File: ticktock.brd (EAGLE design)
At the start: 61 x 67.3 mm, 66 parts, among them IC1 ATMEGA644A, IC2 AD8611, IC3 REF200, IC4 OPA381, J1 ISP PGMR, Q1 MOSFET-NCHANNEL2N7002PW, Q2 MOSFET-NCHANNELBSS138, Q3 MOSFET-NCHANNELBSS138, U1 MAX232, U2 XTAL, U3 FT232, U4 BMP180, X2 DB9 Male

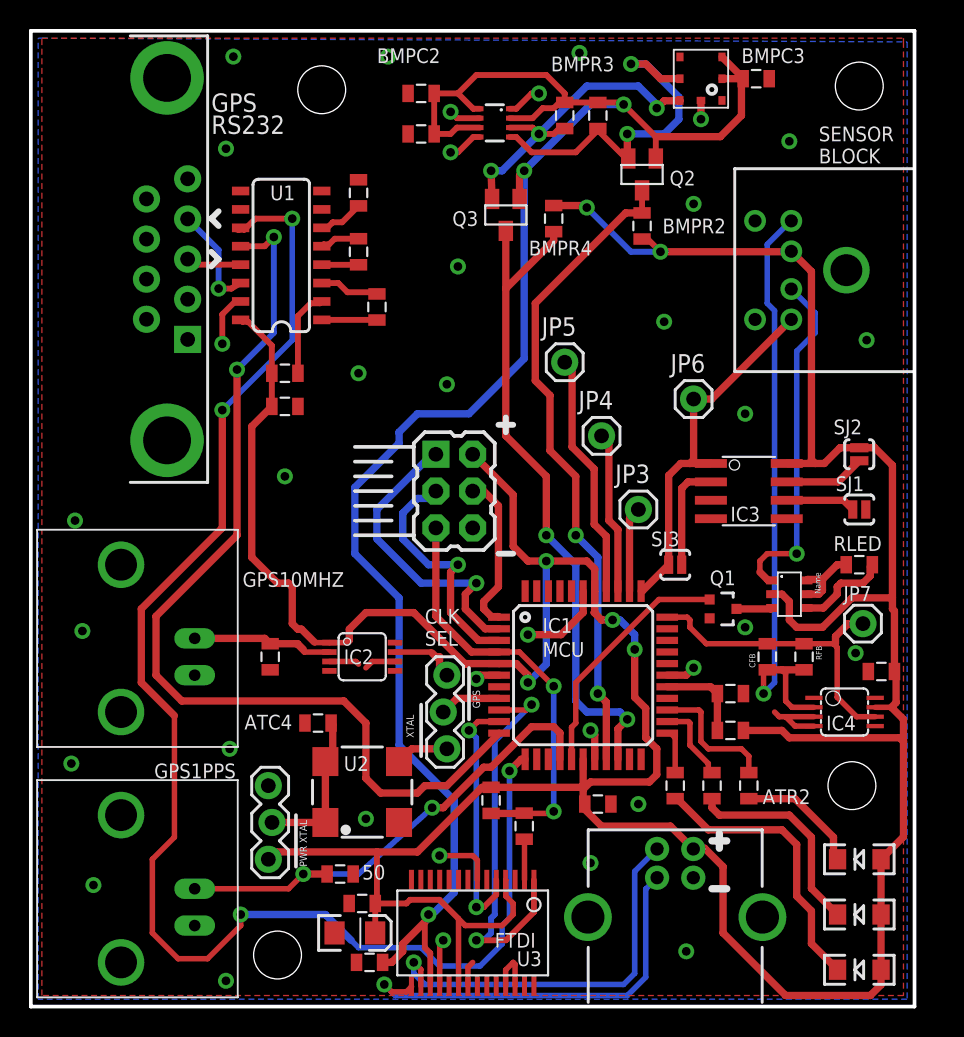
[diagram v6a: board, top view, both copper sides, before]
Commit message: Shuffle tight parts/silkscreens around
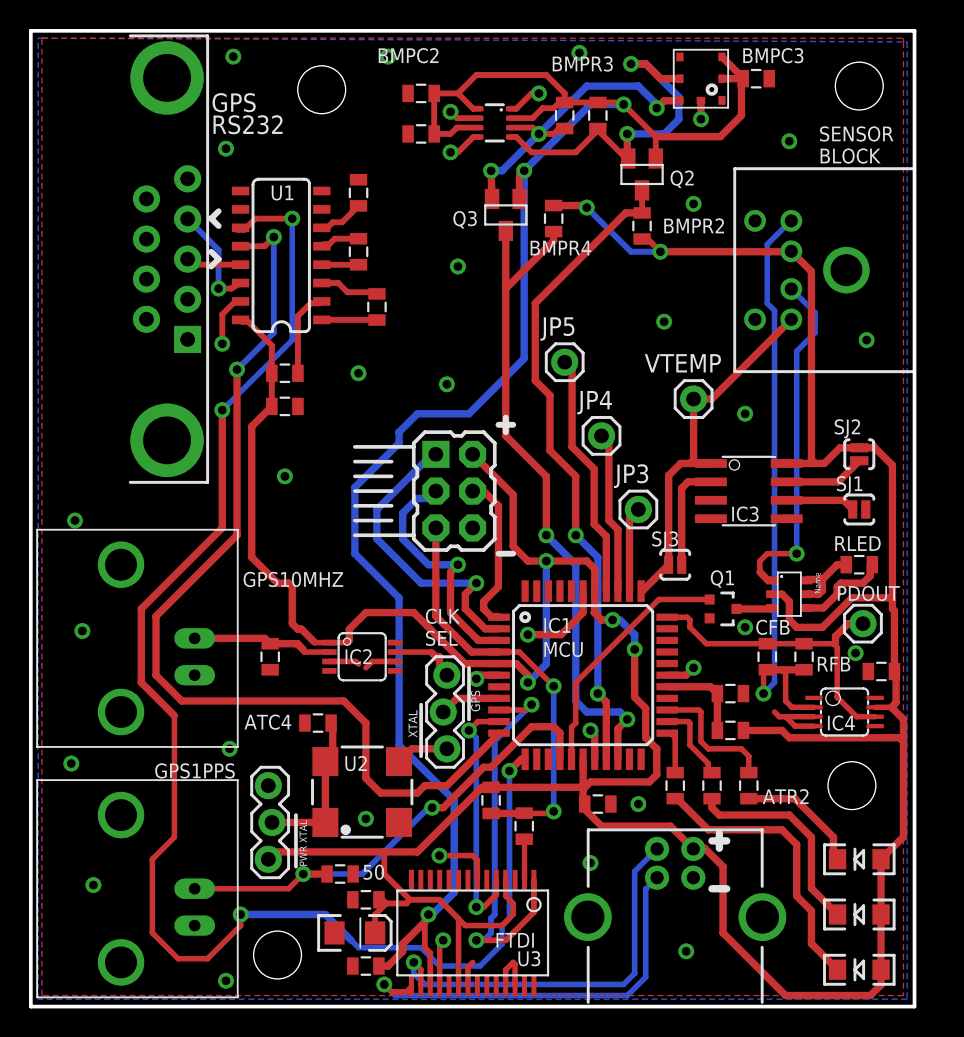
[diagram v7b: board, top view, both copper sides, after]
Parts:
- moved FTC1 0.36 mm to (23.1, 7.37)
- moved FTC3 0.36 mm to (23.1, 2.79)
- renumbered JP6 to VTEMP, JP7 to PDOUT
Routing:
- net 5V: track 272.9 -> 274.0 mm

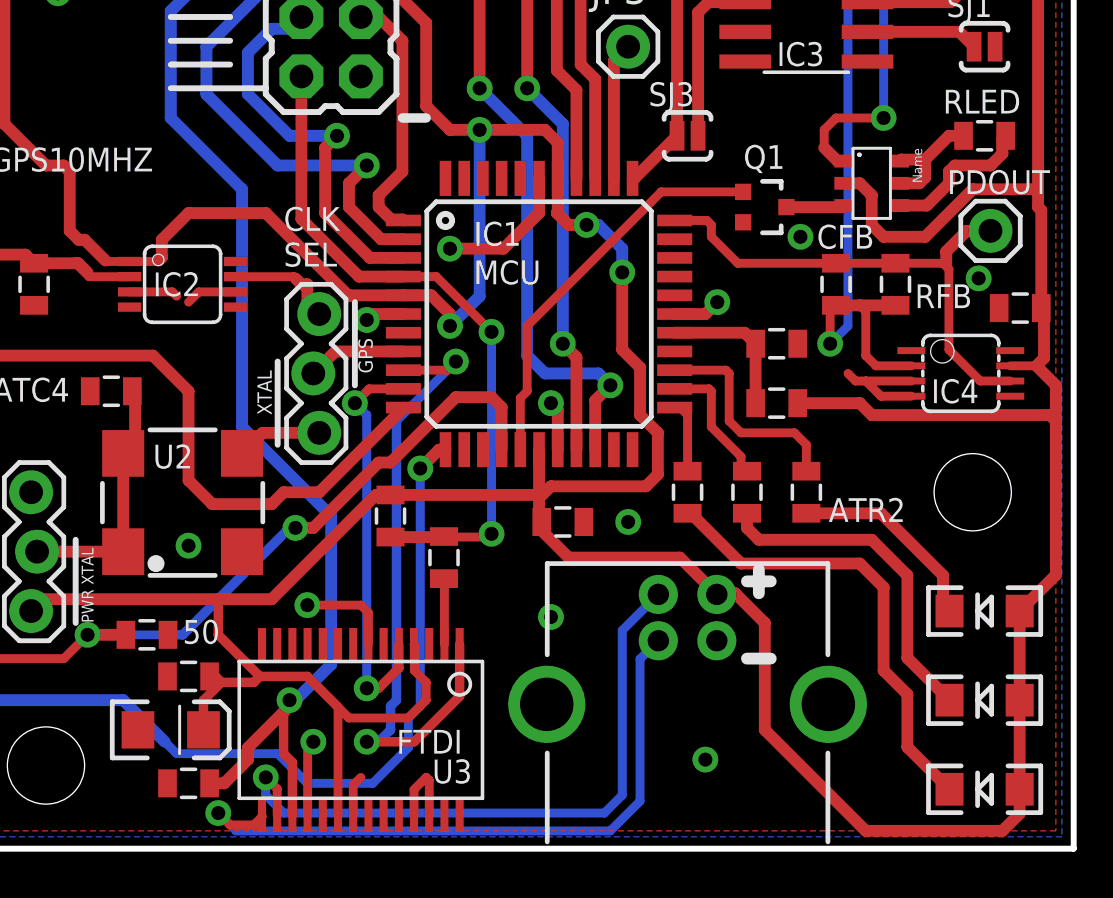
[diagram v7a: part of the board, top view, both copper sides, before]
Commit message: Modify Silkscreen for AL5802
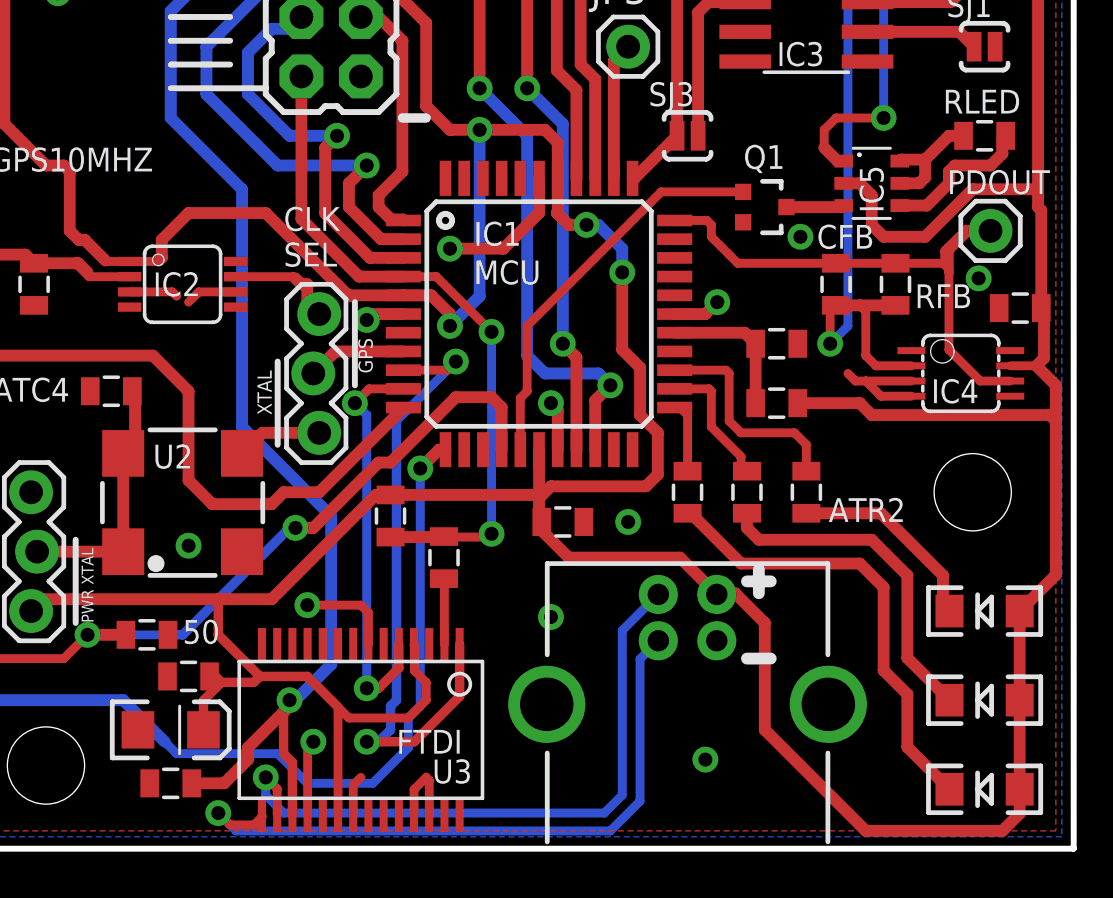
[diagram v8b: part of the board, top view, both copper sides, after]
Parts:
- moved FTC3 0.76 mm to (22.4, 2.79)
- renumbered AL5802 to IC5
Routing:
- net PD_AMP_OUT: track 22.4 -> 23.4 mm
- net 3.3V: track 127.2 -> 128.0 mm
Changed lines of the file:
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@@
 <attribute name="VALUE" x="58.928" y="30.099" size="1.016" layer="27" ratio="20"/>
 </element>
-<element name="AL5802" library="tickTockLibrary" package="AL5802" value="AL5802" x="52.324" y="28.448" smashed="yes" rot="R270"/>
+<element name="IC5" library="tickTockLibrary" package="AL5802" value="AL5802" x="52.324" y="28.448" smashed="yes" rot="R270">
+<attribute name="NAME" x="52.832" y="27.178" size="1.016" layer="25" ratio="20" rot="R90"/>
+</element>
 <element name="PKG-CABLE" library="SparkFun-Connectors" package="MINI-DIN6" value="MINI DIN-6" x="60.96" y="50.8" smashed="yes" rot="R270">
 <attribute name="VALUE" x="50.8" y="56.134" size="1.016" layer="27" ratio="20"/>
@@
 <attribute name="VALUE" x="17.526" y="6.985" size="1.016" layer="27" ratio="20"/>
 </element>
-<element name="FTC3" library="SparkFun-Capacitors" package="0805" value="0.1uF" x="23.114" y="2.794" smashed="yes" rot="R180">
+<element name="FTC3" library="SparkFun-Capacitors" package="0805" value="0.1uF" x="22.352" y="2.794" smashed="yes" rot="R180">
 <attribute name="VALUE" x="19.05" y="0.889" size="1.016" layer="27" ratio="20"/>
 </element>
@@
 <signal name="GND">
 <contactref element="Q1" pad="2"/>
-<contactref element="AL5802" pad="GND"/>
+<contactref element="IC5" pad="GND"/>
 <contactref element="RLED" pad="1"/>
 <contactref element="U1" pad="15"/>
@@
 </signal>
 <signal name="5V">
-<contactref element="AL5802" pad="BIAS"/>
+<contactref element="IC5" pad="BIAS"/>
 <contactref element="PKG-CABLE" pad="1"/>
 <contactref element="U1" pad="16"/>
@@
 <signal name="N$1">
 <contactref element="Q1" pad="3"/>
-<contactref element="AL5802" pad="EN"/>
+<contactref element="IC5" pad="EN"/>
 <wire x1="48.677" y1="27.432" x2="51.058" y2="27.432" width="0.508" layer="1"/>
 <wire x1="51.058" y1="27.432" x2="51.124" y2="27.498" width="0.508" layer="1"/>
 </signal>
 <signal name="N$2">
-<contactref element="AL5802" pad="FB"/>
+<contactref element="IC5" pad="FB"/>
 <contactref element="RLED" pad="2"/>
-<contactref element="AL5802" pad="REXT"/>
+<contactref element="IC5" pad="REXT"/>
 <wire x1="56.25" y1="30.48" x2="55.626" y2="30.48" width="0.508" layer="1"/>
 <wire x1="55.626" y1="30.48" x2="54.61" y2="29.464" width="0.508" layer="1"/>
@@
 </signal>
 <signal name="IR_CATHODE">
-<contactref element="AL5802" pad="OUT"/>
+<contactref element="IC5" pad="OUT"/>
 <contactref element="PKG-CABLE" pad="2"/>
 <wire x1="51.124" y1="29.398" x2="50.866" y2="29.398" width="0.508" layer="1"/>
@@
 <wire x1="27.432" y1="6.096" x2="27.432" y2="6.35" width="0.508" layer="1"/>
 <wire x1="27.178" y1="4.064" x2="27.178" y2="5.842" width="0.4064" layer="1"/>
-<wire x1="24.638" y1="2.794" x2="24.014" y2="2.794" width="0.508" layer="1"/>
+<wire x1="24.638" y1="2.794" x2="23.252" y2="2.794" width="0.508" layer="1"/>
 </signal>
 <signal name="USB_DTR">
@@
 <wire x1="58.246" y1="19.996" x2="56.966" y2="19.996" width="0.381" layer="1"/>
 <wire x1="56.966" y1="19.996" x2="55.626" y2="21.336" width="0.381" layer="1"/>
-<wire x1="55.626" y1="21.336" x2="55.626" y2="24.776" width="0.381" layer="1"/>
+<wire x1="55.626" y1="21.336" x2="55.626" y2="24.638" width="0.381" layer="1"/>
+<wire x1="55.626" y1="24.638" x2="55.626" y2="24.776" width="0.381" layer="1"/>
 <wire x1="55.626" y1="24.776" x2="55.372" y2="25.03" width="0.381" layer="1"/>
 <wire x1="53.34" y1="25.03" x2="50.8" y2="25.03" width="0.381" layer="1"/>
@@
 <wire x1="45.466" y1="26.67" x2="45.466" y2="26.162" width="0.381" layer="1"/>
 <wire x1="55.51" y1="25.03" x2="55.51" y2="25.538" width="0.508" layer="1"/>
-<wire x1="55.51" y1="25.538" x2="56.388" y2="26.416" width="0.508" layer="1"/>
+<wire x1="55.51" y1="25.538" x2="55.626" y2="25.654" width="0.508" layer="1"/>
+<wire x1="55.626" y1="25.654" x2="56.388" y2="26.416" width="0.508" layer="1"/>
 <wire x1="56.388" y1="26.416" x2="57.404" y2="26.416" width="0.508" layer="1"/>
+<wire x1="55.626" y1="25.654" x2="55.626" y2="24.638" width="0.4064" layer="1"/>
 </signal>
 <signal name="VTEMP">
